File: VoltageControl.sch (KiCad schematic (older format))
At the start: 7 parts

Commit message: Initial Annotation
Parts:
- gave numbers to parts that had none: 7
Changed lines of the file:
@@
 $EndDescr
 $Comp
-L R R?
+L R R201
 U 1 1 5B210B9B
 P 2300 4950
-F 0 "R?" V 2380 4950 50  0000 C CNN
+F 0 "R201" V 2380 4950 50  0000 C CNN
 F 1 "R" V 2300 4950 50  0000 C CNN
 F 2 "" V 2230 4950 50  0001 C CNN
@@
 $EndComp
 $Comp
-L LMV358 U?
-U 2 1 5B210BA2
+L LMV358 U201
+U 1 1 5B210BA2
 P 3700 3700
-F 0 "U?" H 3700 3900 50  0000 L CNN
+F 0 "U201" H 3700 3900 50  0000 L CNN
 F 1 "LMV358" H 3700 3500 50  0000 L CNN
 F 2 "" H 3700 3700 50  0001 C CNN
 F 3 "" H 3700 3700 50  0001 C CNN
-	2    3700 3700
+	1    3700 3700
 	1    0    0    -1
 $EndComp
 $Comp
-L GND #PWR?
+L GND #PWR202
 U 1 1 5B210BA9
 P 3600 4150
-F 0 "#PWR?" H 3600 3900 50  0001 C CNN
+F 0 "#PWR202" H 3600 3900 50  0001 C CNN
 F 1 "GND" H 3600 4000 50  0000 C CNN
 F 2 "" H 3600 4150 50  0001 C CNN
@@
 $EndComp
 $Comp
-L POT RV?
+L POT RV201
 U 1 1 5B210BAF
 P 2300 4300
-F 0 "RV?" V 2125 4300 50  0000 C CNN
+F 0 "RV201" V 2125 4300 50  0000 C CNN
 F 1 "POT" V 2200 4300 50  0000 C CNN
 F 2 "" H 2300 4300 50  0001 C CNN
@@
 $EndComp
 $Comp
-L GND #PWR?
+L GND #PWR201
 U 1 1 5B210BB6
 P 3050 3350
-F 0 "#PWR?" H 3050 3100 50  0001 C CNN
+F 0 "#PWR201" H 3050 3100 50  0001 C CNN
 F 1 "GND" H 3050 3200 50  0000 C CNN
 F 2 "" H 3050 3350 50  0001 C CNN
@@
 	3050 3250 3050 3350
 $Comp
-L C C?
+L C C201
 U 1 1 5B210BC7
 P 3050 3100
-F 0 "C?" H 3075 3200 50  0000 L CNN
+F 0 "C201" H 3075 3200 50  0000 L CNN
 F 1 "C" H 3075 3000 50  0000 L CNN
 F 2 "" H 3088 2950 50  0001 C CNN
@@
 	4500 3700 4000 3700
 $Comp
-L D D?
+L D D201
 U 1 1 5B210C37
 P 4650 3700
-F 0 "D?" H 4650 3800 50  0000 C CNN
+F 0 "D201" H 4650 3800 50  0000 C CNN
 F 1 "D" H 4650 3600 50  0000 C CNN
 F 2 "" H 4650 3700 50  0001 C CNN
@@
 $EndComp
 $Comp
-L R R?
+L R R202
 U 1 1 5B210E2B
 P 7200 4150
-F 0 "R?" V 7280 4150 50  0000 C CNN
+F 0 "R202" V 7280 4150 50  0000 C CNN
 F 1 "9K" V 7200 4150 50  0000 C CNN
 F 2 "" V 7130 4150 50  0001 C CNN
@@
 $EndComp
 $Comp
-L R R?
+L R R203
 U 1 1 5B210EF3
 P 7200 4900
-F 0 "R?" V 7280 4900 50  0000 C CNN
+F 0 "R203" V 7280 4900 50  0000 C CNN
 F 1 "1K" V 7200 4900 50  0000 C CNN
 F 2 "" V 7130 4900 50  0001 C CNN

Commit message: Added footprints. Created initial netlist.
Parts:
- C201: footprint (none) -> Capacitors_SMD:C_0805_HandSoldering
- D201: footprint (none) -> Diodes_SMD:D_SOD-523; MPN (none) -> 1N4148WT-7
- R201, R202, R203: footprint (none) -> Resistors_SMD:R_0805
- RV201: footprint (none) -> Potentiometers:Potentiometer_WirePads_largePads
- U201: footprint (none) -> SMD_Packages:SOIC-8-N; MPN (none) -> LMV358IDT
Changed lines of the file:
@@
 F 0 "R201" V 2380 4950 50  0000 C CNN
 F 1 "R" V 2300 4950 50  0000 C CNN
-F 2 "" V 2230 4950 50  0001 C CNN
+F 2 "Resistors_SMD:R_0805" V 2230 4950 50  0001 C CNN
 F 3 "" H 2300 4950 50  0001 C CNN
 	1    2300 4950
@@
 F 0 "U201" H 3700 3900 50  0000 L CNN
 F 1 "LMV358" H 3700 3500 50  0000 L CNN
-F 2 "" H 3700 3700 50  0001 C CNN
+F 2 "SMD_Packages:SOIC-8-N" H 3700 3700 50  0001 C CNN
 F 3 "" H 3700 3700 50  0001 C CNN
+F 4 "LMV358IDT" H 3700 3700 60  0001 C CNN "MPN"
 	1    3700 3700
 	1    0    0    -1
 $EndComp
 $Comp
-L GND #PWR202
+L GND #PWR03
 U 1 1 5B210BA9
 P 3600 4150
-F 0 "#PWR202" H 3600 3900 50  0001 C CNN
+F 0 "#PWR03" H 3600 3900 50  0001 C CNN
 F 1 "GND" H 3600 4000 50  0000 C CNN
 F 2 "" H 3600 4150 50  0001 C CNN
@@
 F 0 "RV201" V 2125 4300 50  0000 C CNN
 F 1 "POT" V 2200 4300 50  0000 C CNN
-F 2 "" H 2300 4300 50  0001 C CNN
+F 2 "Potentiometers:Potentiometer_WirePads_largePads" H 2300 4300 50  0001 C CNN
 F 3 "" H 2300 4300 50  0001 C CNN
 	1    2300 4300
@@
 $EndComp
 $Comp
-L GND #PWR201
+L GND #PWR04
 U 1 1 5B210BB6
 P 3050 3350
-F 0 "#PWR201" H 3050 3100 50  0001 C CNN
+F 0 "#PWR04" H 3050 3100 50  0001 C CNN
 F 1 "GND" H 3050 3200 50  0000 C CNN
 F 2 "" H 3050 3350 50  0001 C CNN
@@
 F 0 "C201" H 3075 3200 50  0000 L CNN
 F 1 "C" H 3075 3000 50  0000 L CNN
-F 2 "" H 3088 2950 50  0001 C CNN
+F 2 "Capacitors_SMD:C_0805_HandSoldering" H 3088 2950 50  0001 C CNN
 F 3 "" H 3050 3100 50  0001 C CNN
 	1    3050 3100
@@
 F 0 "D201" H 4650 3800 50  0000 C CNN
 F 1 "D" H 4650 3600 50  0000 C CNN
-F 2 "" H 4650 3700 50  0001 C CNN
+F 2 "Diodes_SMD:D_SOD-523" H 4650 3700 50  0001 C CNN
 F 3 "" H 4650 3700 50  0001 C CNN
+F 4 "1N4148WT-7" H 4650 3700 60  0001 C CNN "MPN"
 	1    4650 3700
 	1    0    0    -1
@@
 F 0 "R202" V 7280 4150 50  0000 C CNN
 F 1 "9K" V 7200 4150 50  0000 C CNN
-F 2 "" V 7130 4150 50  0001 C CNN
+F 2 "Resistors_SMD:R_0805" V 7130 4150 50  0001 C CNN
 F 3 "" H 7200 4150 50  0001 C CNN
 	1    7200 4150
@@
 F 0 "R203" V 7280 4900 50  0000 C CNN
 F 1 "1K" V 7200 4900 50  0000 C CNN
-F 2 "" V 7130 4900 50  0001 C CNN
+F 2 "Resistors_SMD:R_0805" V 7130 4900 50  0001 C CNN
 F 3 "" H 7200 4900 50  0001 C CNN
 	1    7200 4900

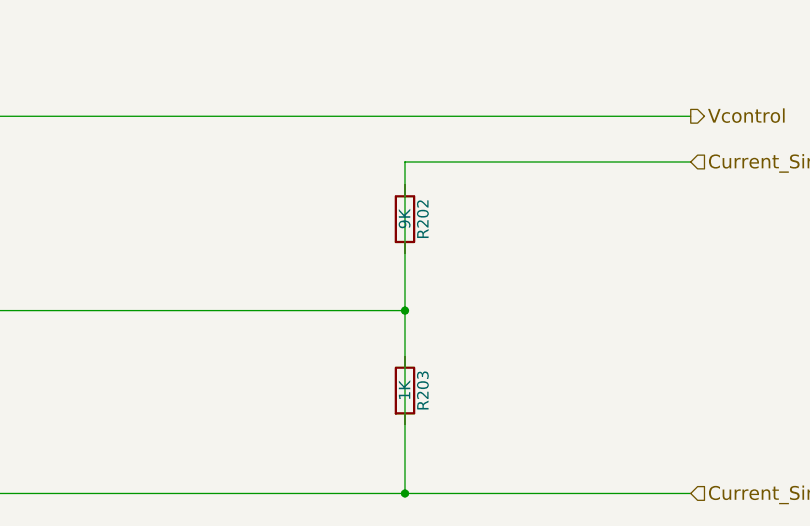
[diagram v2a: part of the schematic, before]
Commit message: Update connector footprints
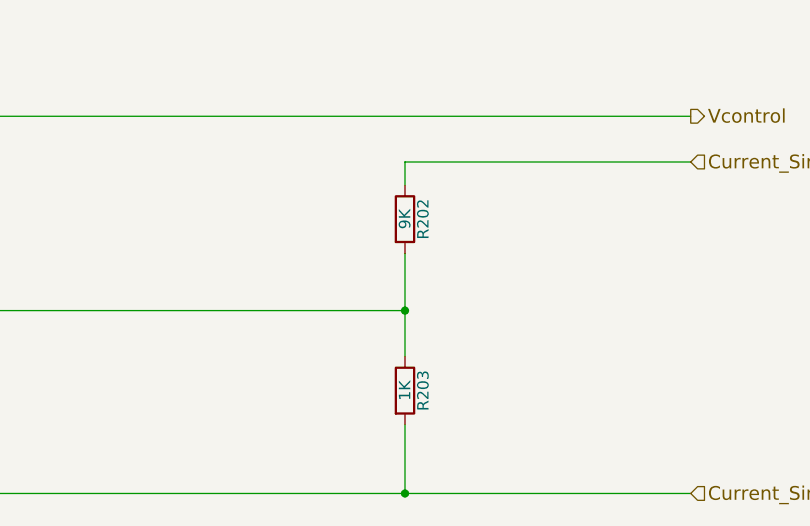
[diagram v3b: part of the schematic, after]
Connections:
- wire segments 21 -> 23
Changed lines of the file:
@@
 	2300 5350 8450 5350
 Wire Wire Line
-	3600 4000 3600 4150
-Wire Wire Line
 	2500 4300 2450 4300
-Wire Wire Line
-	3600 2850 3600 3400
 Wire Wire Line
 	2500 2850 3600 2850
@@
 Vcontrol
 Wire Wire Line
-	7200 5350 7200 3900
-Wire Wire Line
 	7200 3900 8450 3900
 Text HLabel 8450 3900 2    60   Input ~ 0
@@
 Current_Sink-
 Connection ~ 7200 5350
+Wire Wire Line
+	7200 3900 7200 4000
+Wire Wire Line
+	7200 4300 7200 4750
+Wire Wire Line
+	7200 5050 7200 5350
+Wire Wire Line
+	3600 2850 3600 3400
+Wire Wire Line
+	3600 4000 3600 4150
 $EndSCHEMATC

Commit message: Fixed divider resistors and found valus. Added pot footprint.
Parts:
- R201: value R -> 28.7K
- RV201: value POT -> 10K; footprint Potentiometers:Potentiometer_WirePads_largePads -> Current:P090L-02F25BR10K
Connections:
- wire segments 23 -> 22
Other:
- note added: "0-20V"
- note added: "0-2V"
- moved on the sheet: C201, R201
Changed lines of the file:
@@
 L R R201
 U 1 1 5B210B9B
-P 2300 4950
-F 0 "R201" V 2380 4950 50  0000 C CNN
-F 1 "R" V 2300 4950 50  0000 C CNN
-F 2 "Resistors_SMD:R_0805" V 2230 4950 50  0001 C CNN
-F 3 "" H 2300 4950 50  0001 C CNN
-	1    2300 4950
+P 2500 3550
+F 0 "R201" V 2580 3550 50  0000 C CNN
+F 1 "28.7K" V 2500 3550 50  0000 C CNN
+F 2 "Resistors_SMD:R_0805" V 2430 3550 50  0001 C CNN
+F 3 "" H 2500 3550 50  0001 C CNN
+	1    2500 3550
 	1    0    0    -1
 $EndComp
@@
 P 2300 4300
 F 0 "RV201" V 2125 4300 50  0000 C CNN
-F 1 "POT" V 2200 4300 50  0000 C CNN
-F 2 "Potentiometers:Potentiometer_WirePads_largePads" H 2300 4300 50  0001 C CNN
+F 1 "10K" V 2200 4300 50  0000 C CNN
+F 2 "Current:P090L-02F25BR10K" H 2300 4300 50  0001 C CNN
 F 3 "" H 2300 4300 50  0001 C CNN
 	1    2300 4300
@@
 L GND #PWR04
 U 1 1 5B210BB6
-P 3050 3350
-F 0 "#PWR04" H 3050 3100 50  0001 C CNN
-F 1 "GND" H 3050 3200 50  0000 C CNN
-F 2 "" H 3050 3350 50  0001 C CNN
-F 3 "" H 3050 3350 50  0001 C CNN
-	1    3050 3350
+P 3050 3075
+F 0 "#PWR04" H 3050 2825 50  0001 C CNN
+F 1 "GND" H 3050 2925 50  0000 C CNN
+F 2 "" H 3050 3075 50  0001 C CNN
+F 3 "" H 3050 3075 50  0001 C CNN
+	1    3050 3075
 	1    0    0    -1
 $EndComp
@@
 	3150 4550 7200 4550
 Wire Wire Line
-	2300 4450 2300 4800
-Wire Wire Line
-	2300 5100 2300 5350
+	2300 4450 2300 5350
 Wire Wire Line
 	2300 5350 8450 5350
 Wire Wire Line
-	2500 4300 2450 4300
+	2450 4300 2750 4300
 Wire Wire Line
-	2500 2850 3600 2850
+	1550 2525 3600 2525
 Wire Wire Line
-	3050 3250 3050 3350
+	3050 2975 3050 3075
 $Comp
 L C C201
 U 1 1 5B210BC7
-P 3050 3100
-F 0 "C201" H 3075 3200 50  0000 L CNN
-F 1 "C" H 3075 3000 50  0000 L CNN
-F 2 "Capacitors_SMD:C_0805_HandSoldering" H 3088 2950 50  0001 C CNN
-F 3 "" H 3050 3100 50  0001 C CNN
-	1    3050 3100
+P 3050 2825
+F 0 "C201" H 3075 2925 50  0000 L CNN
+F 1 "C" H 3075 2725 50  0000 L CNN
+F 2 "Capacitors_SMD:C_0805_HandSoldering" H 3088 2675 50  0001 C CNN
+F 3 "" H 3050 2825 50  0001 C CNN
+	1    3050 2825
 	1    0    0    -1
 $EndComp
-Connection ~ 3050 2850
-Connection ~ 2500 2850
-Wire Wire Line
-	3050 2950 3050 2850
-Connection ~ 2300 4600
+Connection ~ 3050 2525
 Wire Wire Line
 	2750 3600 3400 3600
-Wire Wire Line
-	2750 4600 2300 4600
-Wire Wire Line
-	2750 3600 2750 4600
-Text GLabel 1550 2300 0    60   Input ~ 0
+Text GLabel 1550 2525 0    60   Input ~ 0
 2.7V
-Wire Wire Line
-	1550 2300 2500 2300
-Connection ~ 2500 2300
-Wire Wire Line
-	2500 2300 2500 4300
 Wire Wire Line
 	4500 3700 4000 3700
@@
 	7200 5050 7200 5350
 Wire Wire Line
-	3600 2850 3600 3400
+	3600 2525 3600 3400
 Wire Wire Line
 	3600 4000 3600 4150
+Wire Wire Line
+	2500 3700 2500 3700
+Wire Wire Line
+	2500 3700 2500 4300
+Wire Wire Line
+	2500 3400 2500 2525
+Connection ~ 2500 2525
+Wire Wire Line
+	2750 4300 2750 3600
+Connection ~ 2500 4300
+Text Notes 2950 3575 0    60   ~ 0
+0-2V
+Wire Wire Line
+	3050 2675 3050 2525
+Text Notes 5950 4525 0    60   ~ 0
+0-2V
+Text Notes 7725 3875 0    60   ~ 0
+0-20V
 $EndSCHEMATC
